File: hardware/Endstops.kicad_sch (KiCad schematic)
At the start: 47 parts

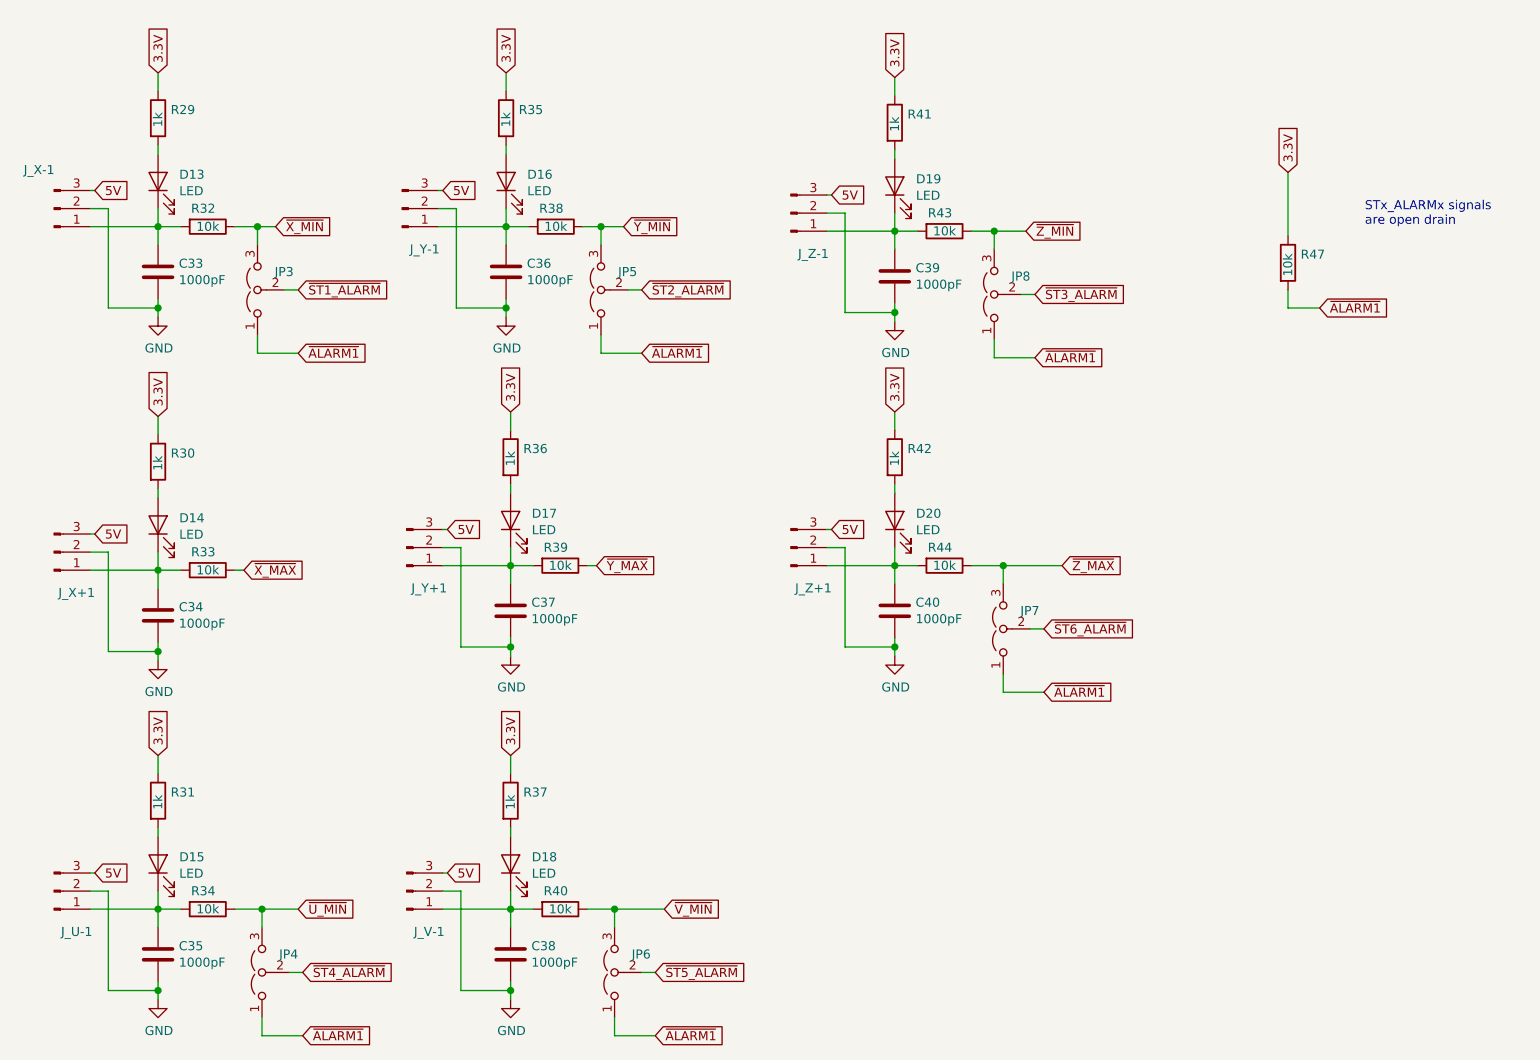
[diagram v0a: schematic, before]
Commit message: Add more input protection. 480 ohm resistors on all direct IO pins. Clamping diodes on the endstops.
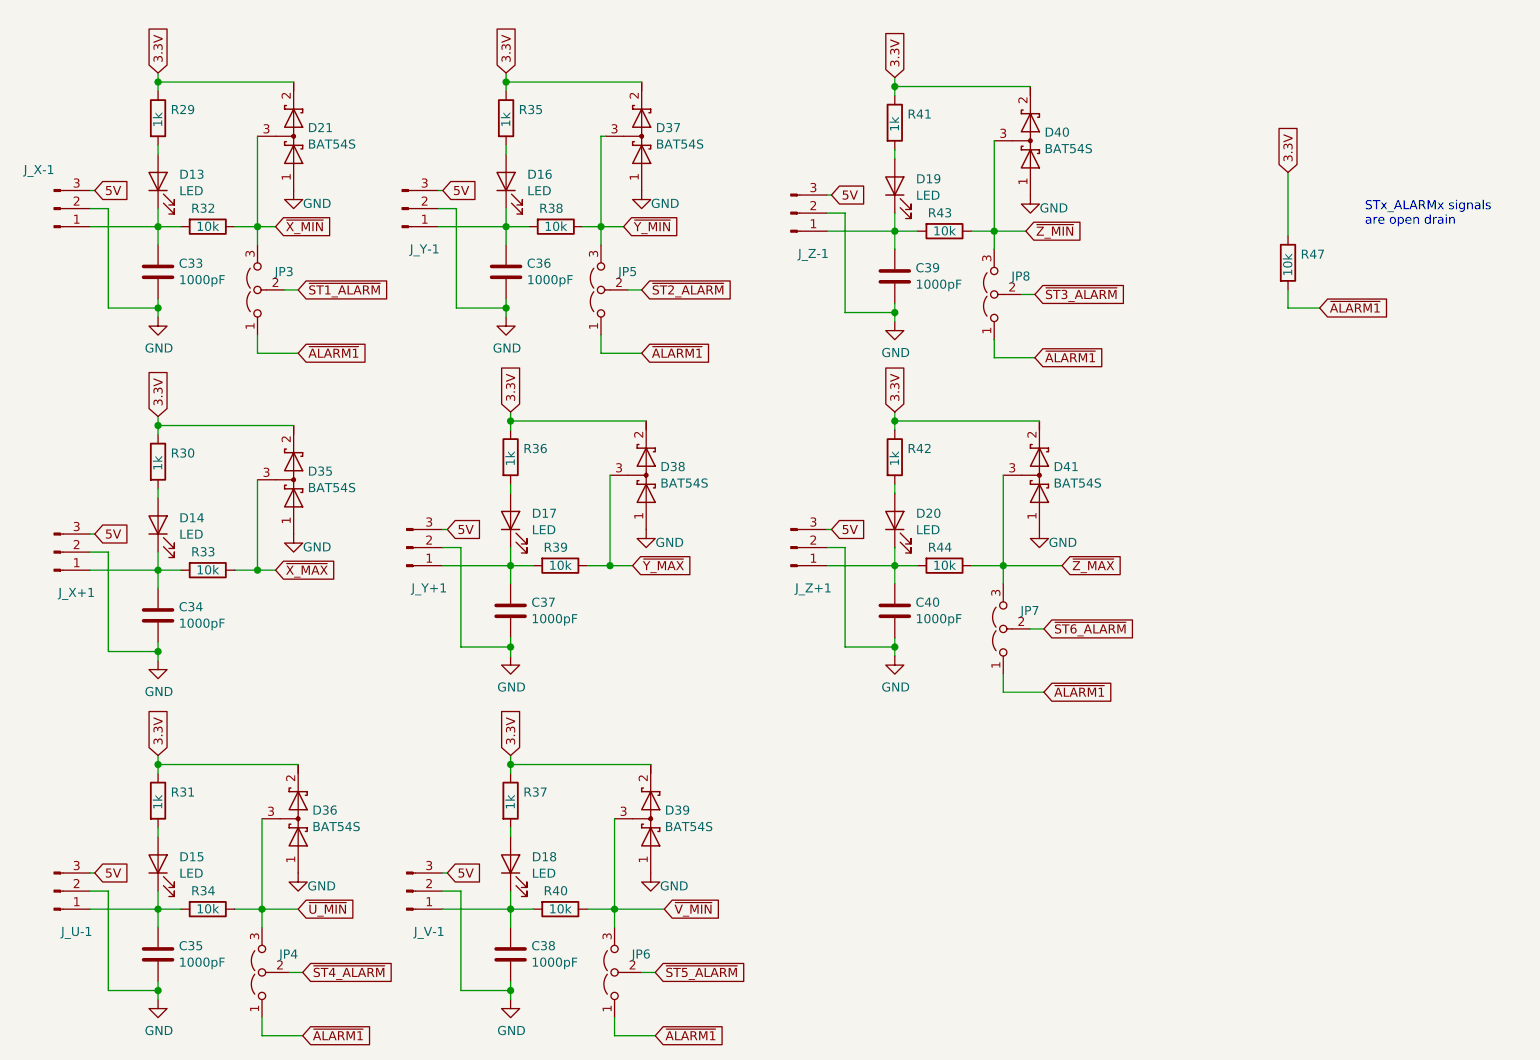
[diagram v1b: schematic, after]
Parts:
- added D21, D35, D36, D37, D38, D39, D40, D41: BAT54S, Package_TO_SOT_SMD:SOT-23, symbol Device:D_Schottky_x2_Serial_AKC
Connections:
- net 3.3V: now also D21.2 (K), D35.2 (K), D36.2 (K), D37.2 (K), D38.2 (K), D39.2 (K), D40.2 (K), D41.2 (K)
- net GND: now also D21.1 (A), D35.1 (A), D36.1 (A), D37.1 (A), D38.1 (A), D39.1 (A), D40.1 (A), D41.1 (A)
- net ~U_MIN: now also D36.3 (common)
- net ~V_MIN: now also D39.3 (common)
- net ~X_MAX: now also D35.3 (common)
- net ~X_MIN: now also D21.3 (common)
- net ~Y_MAX: now also D38.3 (common)
- net ~Y_MIN: now also D37.3 (common)
- net ~Z_MAX: now also D41.3 (common)
- net ~Z_MIN: now also D40.3 (common)

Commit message: Revert "Add more input protection. 480 ohm resistors on all direct IO pins."
This reverts commit 49fdbd5165b8c1709549cdf3235e4b40c9a44330.
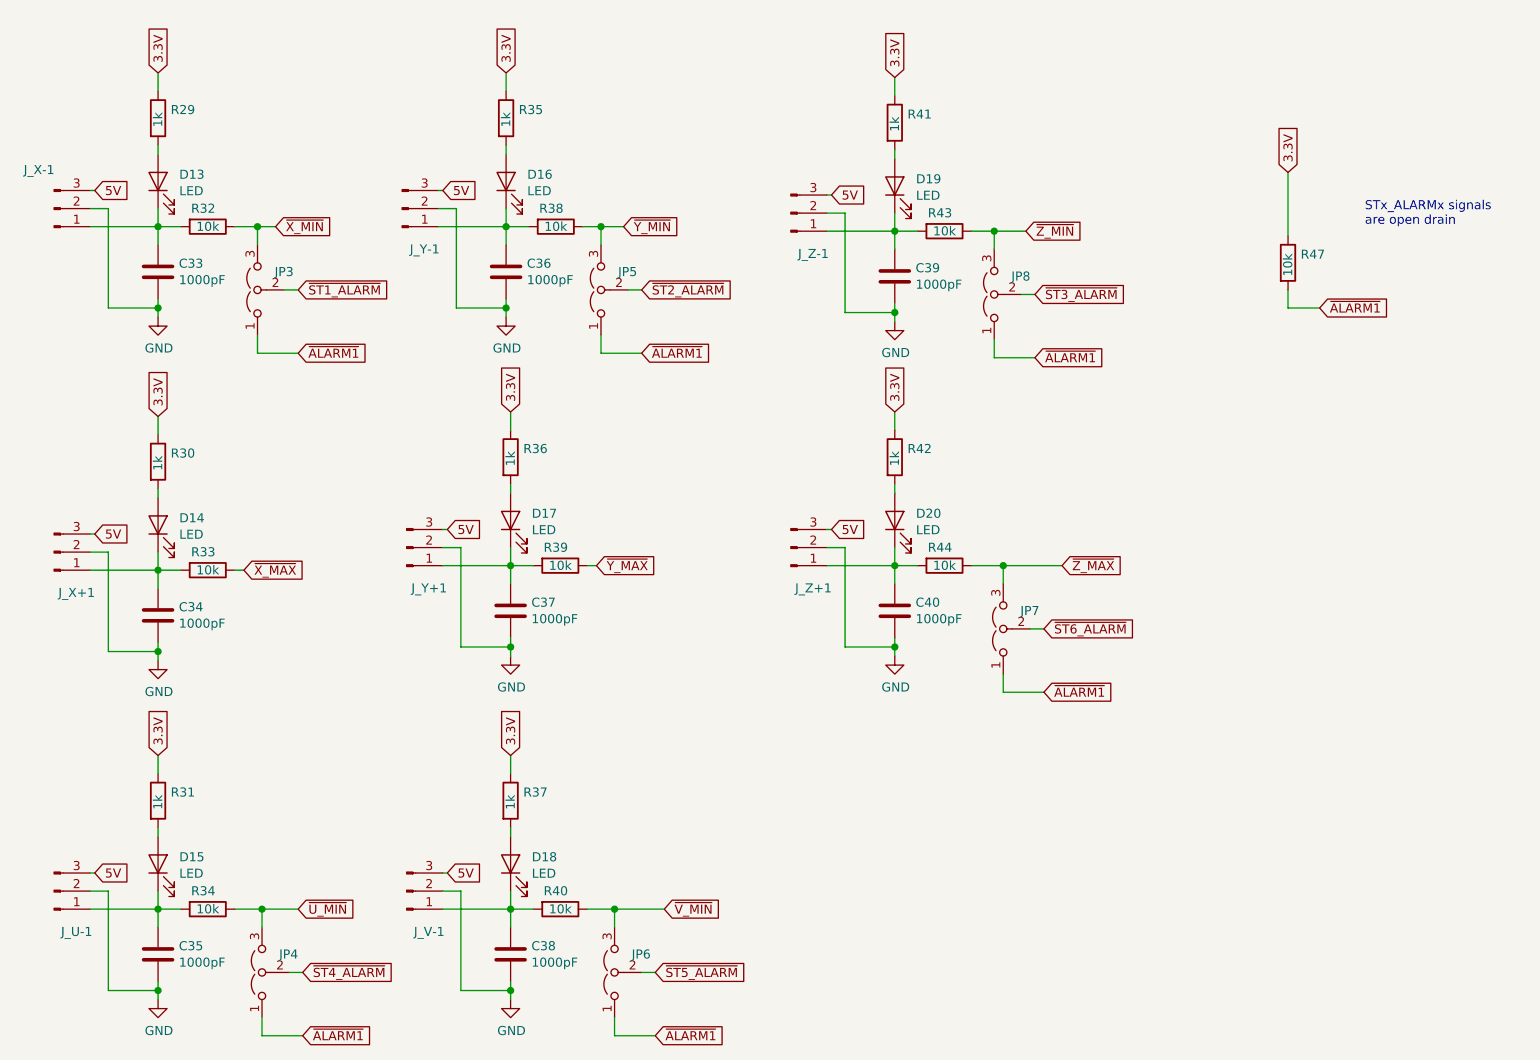
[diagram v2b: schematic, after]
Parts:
- removed D21, D35, D36, D37, D38, D39, D40, D41: BAT54S, Package_TO_SOT_SMD:SOT-23, symbol Device:D_Schottky_x2_Serial_AKC
